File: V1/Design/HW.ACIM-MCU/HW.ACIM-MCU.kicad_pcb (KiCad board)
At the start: 4 copper layers, 39.1 x 39.2 mm, 41 parts, among them J1 HEADER 2x15POS, J2 HEADER 2x15POS, U1 MIPS 32-bit DSC, U2 12MHz (3225), X1 32.768kHz

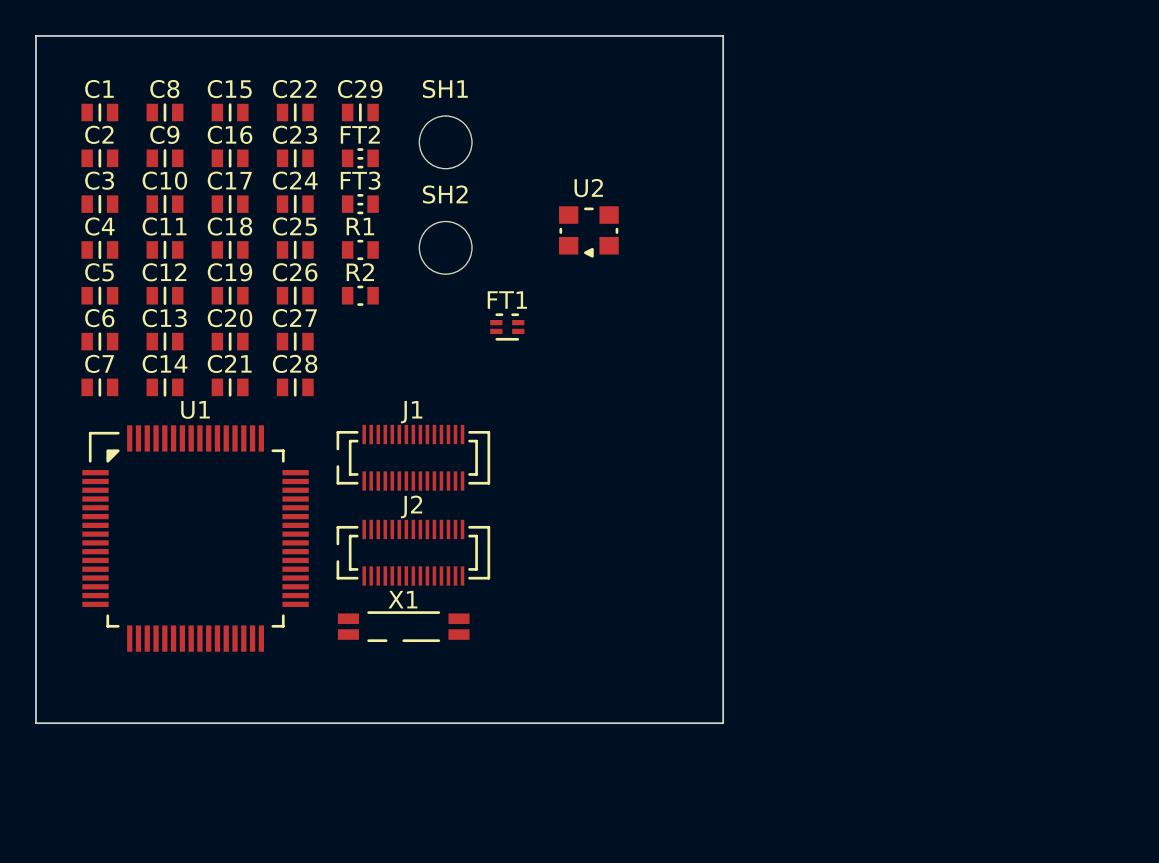
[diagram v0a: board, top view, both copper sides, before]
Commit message: MCU PIM schematic update 3
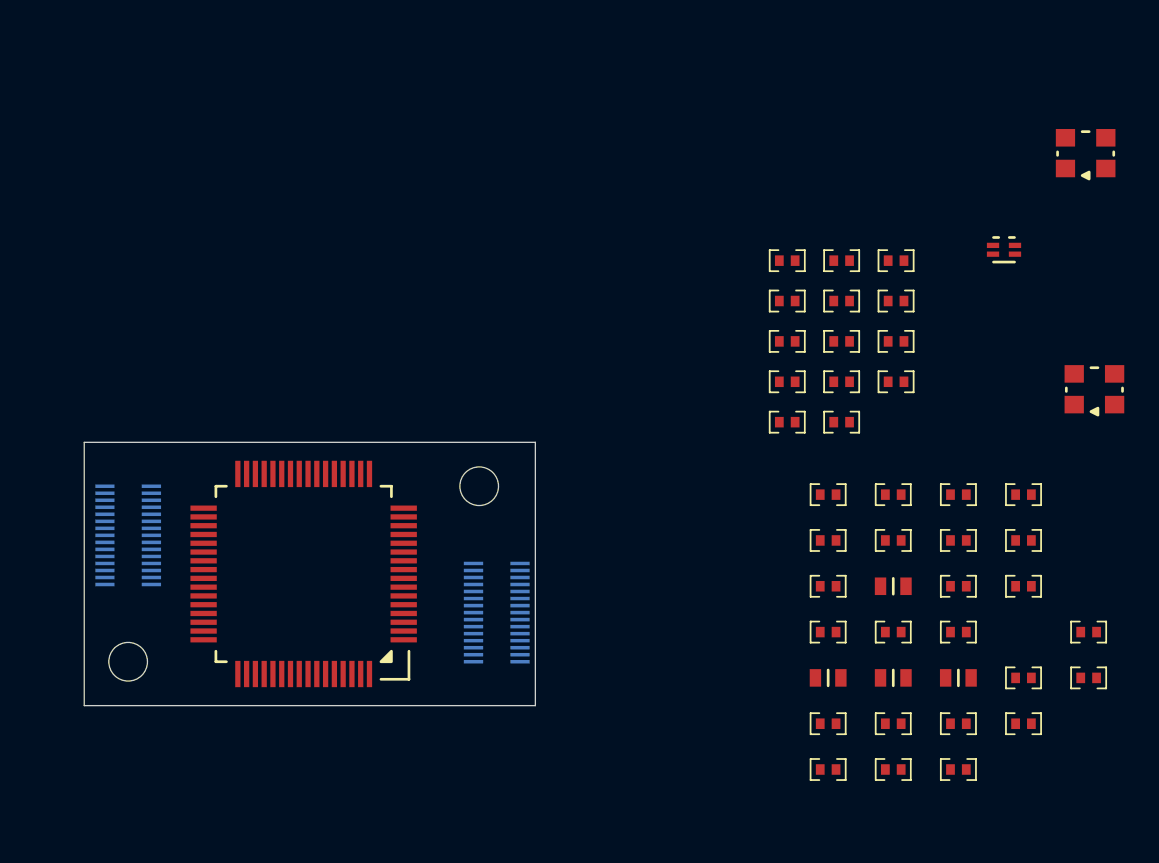
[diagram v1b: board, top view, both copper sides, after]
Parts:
- removed C25: 22pF, SAMPI:CAP0603
- removed C28, C29: 9pF, SAMPI:CAP0603
- removed FT2, FT3: 120R@100MHz, SAMPI:FT0603
- removed X1: 32.768kHz, SAMPI:SMD4-7015
- added R10: 10R, SAMPI:RES0402, F.Cu at (128.0, 90.9)
- added R11: 10R, SAMPI:RES0402, F.Cu at (128.0, 93.2)
- added R12: 10R, SAMPI:RES0402, F.Cu at (128.0, 95.5)
- added R13: 10R, SAMPI:RES0402, F.Cu at (131.1, 86.3)
- added R14: 10R, SAMPI:RES0402, F.Cu at (131.1, 88.6)
- added R15: 10K, SAMPI:RES0402, F.Cu at (131.1, 90.9)
- added R16: 10R, SAMPI:RES0402, F.Cu at (131.1, 93.2)
- added R3: 10R, SAMPI:RES0402, F.Cu at (124.9, 86.3)
- added R4: 10R, SAMPI:RES0402, F.Cu at (124.9, 88.6)
- added R5: 10R, SAMPI:RES0402, F.Cu at (124.9, 90.9)
- added R6: 10R, SAMPI:RES0402, F.Cu at (124.9, 93.2)
- added R7: 10R, SAMPI:RES0402, F.Cu at (124.9, 95.5)
- added R8: 10R, SAMPI:RES0402, F.Cu at (128.0, 86.3)
- added R9: 10R, SAMPI:RES0402, F.Cu at (128.0, 88.6)
- added U3: 32.768kHz, SAMPI:CDFN3225-4LD-PL-1, F.Cu at (142.4, 93.7)
- C1, C11, C13, C14, C15, C17, C18, C2, C20, C21, C22, C23, C24, C26, C27, C3, C4, C6, C7, C8, C9: footprint SAMPI:CAP0603 -> SAMPI:CAP0402
- C12, C5: value 22pF -> 15pF
- C16: value 22pF -> 100nF; footprint SAMPI:CAP0603 -> SAMPI:CAP0402
- J1, J2: moved to B.Cu
- R1: value 0R -> 10K; footprint SAMPI:RES0603 -> SAMPI:RES0402
- R2: value 100K -> 10R; footprint SAMPI:RES0603 -> SAMPI:RES0402
- SH1, SH2: footprint Liem:HOLDER-3MM -> Liem:HOLDER-2.2MM
- U2: value 12MHz (3225) -> 24MHz
- moved C10 46.9 mm to (130.9, 104.9)
- moved C11 46.9 mm to (130.9, 107.5)
- moved C8 46.9 mm to (130.9, 99.6)
- moved C9 46.9 mm to (130.9, 102.2)
- moved R1 46.9 mm to (142.1, 107.5)
- moved C1 46.9 mm to (127.2, 99.6)
- moved C12 46.9 mm to (130.9, 110.1)
- moved C13 46.9 mm to (130.9, 112.7)
- moved C14 46.9 mm to (130.9, 115.3)
- moved C15 46.9 mm to (134.6, 99.6)
- moved C16 46.9 mm to (134.6, 102.2)
- moved C17 46.9 mm to (134.6, 104.9)
- moved C18 46.9 mm to (134.6, 107.5)
- moved C2 46.9 mm to (127.2, 102.2)
- moved C22 46.9 mm to (138.3, 99.6)
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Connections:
- C1 pad 2: /VREF_SENSE -> /VAC_DIV
- C10 pad 1: GND -> AGND
- C10 pad 2: Net-(U1-AVDD) -> AVDD
- C11 pad 2: VDD -> +3V3
- C12 pad 2: Net-(U1-AVDD) -> /RTC_CLK
- C13 pad 2: VDD -> +3V3
- C15 pad 2: /MC_IPM_TEMP -> /MC_IW
- C16 pad 2: VREF -> +3V3
- C17 pad 2: /MC_IU_SENSE -> /MC_IV
- C18 pad 2: /MC_VDC_SENSE -> /MC_VV_DIV
- C19 pad 2: VDD -> +3V3
- C2 pad 2: /PFC_IA_SENSE -> /PFC_IB
- C20 pad 2: /MC_IV_SENSE -> /MC_IU
- C21 pad 2: /MC_VU_SENSE -> /MC_VU_DIV
- C22 pad 1: GND -> AGND
- C22 pad 2: VDD -> /MC_VR_DIV
- C23 pad 2: /MC_IW_SENSE -> /MC_TEMP
- C24 pad 2: /MC_VV_SENSE -> /MC_VDC_DIV
- C26 pad 2: /MC_IDC_SENSE -> /MC_VW_DIV
- C27 pad 2: /MC_VW_SENSE -> /MC_IDC_DIV
- C3 pad 2: /PFC_IB_SENSE -> /PFC_IA
- C4 pad 2: /VAC_SENSE -> /VREF_DIV
- C7 pad 2: VDD -> +3V3
- C8 pad 2: VDD -> +3V3
- C9 pad 2: Net-(U1-AVDD) -> AVDD
- J1 pad 1: unconnected-(J1-Pad1) -> GND
- J1 pad 10: unconnected-(J1-Pad10) -> /TXD1
- J1 pad 11: unconnected-(J1-Pad11) -> /RXD2
- J1 pad 12: unconnected-(J1-Pad12) -> /TXD2
- J1 pad 13: unconnected-(J1-Pad13) -> /IND_ERR
- J1 pad 14: unconnected-(J1-Pad14) -> /IND_RUN
- J1 pad 15: unconnected-(J1-Pad15) -> /MC_PWM_WL
- J1 pad 16: unconnected-(J1-Pad16) -> /MC_PWM_WH
- J1 pad 17: unconnected-(J1-Pad17) -> /MC_PWM_VL
- J1 pad 18: unconnected-(J1-Pad18) -> /MC_PWM_VH
- J1 pad 19: unconnected-(J1-Pad19) -> /MC_PWM_UL
- J1 pad 2: unconnected-(J1-Pad2) -> /PGD
- J1 pad 20: unconnected-(J1-Pad20) -> /MC_PWM_UH
- J1 pad 21: unconnected-(J1-Pad21) -> /~{INV_FLT}
- J1 pad 22: unconnected-(J1-Pad22) -> /MC_VR_SENSE
- J1 pad 23: unconnected-(J1-Pad23) -> /VREF_SENSE
- J1 pad 24: unconnected-(J1-Pad24) -> /MC_TEMP_SENSE
- J1 pad 25: unconnected-(J1-Pad25) -> /MC_IU_SENSE
- J1 pad 26: unconnected-(J1-Pad26) -> /MC_VW_SENSE
- J1 pad 27: unconnected-(J1-Pad27) -> /MC_IV_SENSE
- J1 pad 28: unconnected-(J1-Pad28) -> /MC_VV_SENSE
- J1 pad 29: unconnected-(J1-Pad29) -> /MC_IW_SENSE
- J1 pad 3: unconnected-(J1-Pad3) -> /USB_P
- J1 pad 30: unconnected-(J1-Pad30) -> /MC_VU_SENSE
- J1 pad 4: unconnected-(J1-Pad4) -> /PGC
- J1 pad 5: unconnected-(J1-Pad5) -> /USB_N
- J1 pad 6: unconnected-(J1-Pad6) -> /~{MCLR}
- J1 pad 7: unconnected-(J1-Pad7) -> /VBUS
- J1 pad 8: unconnected-(J1-Pad8) -> /~{BT_UBT}
- J1 pad 9: unconnected-(J1-Pad9) -> /RXD1
- J2 pad 1: unconnected-(J2-Pad1) -> GND
- J2 pad 11: unconnected-(J2-Pad11) -> /SDO
- J2 pad 12: unconnected-(J2-Pad12) -> /SDI
- J2 pad 13: unconnected-(J2-Pad13) -> /~{MEM_CFG}
- J2 pad 14: unconnected-(J2-Pad14) -> /SCK
- J2 pad 15: unconnected-(J2-Pad15) -> /GPIO2
- J2 pad 16: unconnected-(J2-Pad16) -> /GPIO1
- J2 pad 17: unconnected-(J2-Pad17) -> /PFC_PWM_ENB
- J2 pad 18: unconnected-(J2-Pad18) -> /PFC_PWM_B
- J2 pad 19: unconnected-(J2-Pad19) -> /PFC_PWM_ENA
- J2 pad 2: unconnected-(J2-Pad2) -> GND
- J2 pad 20: unconnected-(J2-Pad20) -> /PFC_PWM_A
- J2 pad 21: unconnected-(J2-Pad21) -> /PFC_IA_SENSE
- J2 pad 22: unconnected-(J2-Pad22) -> /~{PFC_FLT}
- J2 pad 23: unconnected-(J2-Pad23) -> /VAC_SENSE
- J2 pad 24: unconnected-(J2-Pad24) -> /PFC_IB_SENSE
- J2 pad 25: unconnected-(J2-Pad25) -> /MC_VDC_SENSE
- J2 pad 26: unconnected-(J2-Pad26) -> /MC_IDC_SENSE
- J2 pad 27: unconnected-(J2-Pad27) -> /ENC_HOME
- J2 pad 28: unconnected-(J2-Pad28) -> /ENC_A
- J2 pad 29: unconnected-(J2-Pad29) -> /ENC_INDEX
- J2 pad 3: unconnected-(J2-Pad3) -> +3V3
- J2 pad 30: unconnected-(J2-Pad30) -> /ENC_B
- J2 pad 4: unconnected-(J2-Pad4) -> +3V3
- J2 pad 5: unconnected-(J2-Pad5) -> AGND
- J2 pad 6: unconnected-(J2-Pad6) -> AGND
- J2 pad 7: unconnected-(J2-Pad7) -> VREF
- J2 pad 8: unconnected-(J2-Pad8) -> VREF
- R1 pad 1: /SYS_CLK -> Net-(U2-EN)
- R1 pad 2: Net-(U2-CLKO) -> +3V3
- R2 pad 1: /VBUS -> /MC_TEMP_SENSE
- R2 pad 2: GND -> /MC_TEMP
- U1 pad 1: /IND_RUN -> unconnected-(U1-TCK/RPA7/PWM10H/PWM4L/PMD5/RA7-Pad1)
- U1 pad 10: VDD -> +3V3
- U1 pad 11: /MC_VDC_SENSE -> /MC_TEMP
- U1 pad 12: /MC_IDC_SENSE -> /PFC_IA
- U1 pad 13: /MC_IU_SENSE -> /PFC_IB
- U1 pad 14: /MC_IV_SENSE -> /MC_IU
- U1 pad 15: /MC_IW_SENSE -> /MC_IV
- U1 pad 16: /MC_VU_SENSE -> /MC_IW
- U1 pad 19: Net-(U1-AVDD) -> AVDD
- U1 pad 21: /MC_VW_SENSE -> /MC_VV_DIV
- U1 pad 22: /MC_VV_SENSE -> /MC_VU_DIV
- U1 pad 23: /MC_IPM_TEMP -> /MC_VW_DIV
- U1 pad 24: /VREF_SENSE -> /VREF_DIV
- U1 pad 26: VDD -> +3V3
- U1 pad 27: /PFC_IA_SENSE -> unconnected-(U1-AN12/CVD12/C2IN2-/C5IN2-/SDA4/FLT5/PMA11/RE12-Pad27)
- U1 pad 28: /PFC_IB_SENSE -> unconnected-(U1-AN13/CVD13/C3IN2-/FLT6/SCL4/PMA10/RE13-Pad28)
- U1 pad 32: /~{MEM_TMP} -> unconnected-(U1-FLT15/RPB4/SCL2/PMA8/RB4-Pad32)
- U1 pad 33: /~{MEM_CFG} -> /MC_VR_DIV
- U1 pad 35: VDD -> +3V3
- U1 pad 38: VDD -> +3V3
- U1 pad 40: /SYS_CLK_EN -> unconnected-(U1-OSCO/CLKO/RPC15/RC15-Pad40)
- U1 pad 42: /~{BT_UBT} -> unconnected-(U1-RD8-Pad42)
- U1 pad 45: /TXD2 -> /MC_VDC_DIV
- U1 pad 46: /TXD1 -> /VAC_DIV
- U1 pad 47: /SOSCI -> /RTC_CLK
- U1 pad 48: /SOSCO -> unconnected-(U1-SOSCO/T1CK/RPB8/RB8-Pad48)
- U1 pad 49: /VAC_SENSE -> /MC_IDC
- U1 pad 57: VDD -> +3V3
- U1 pad 64: /IND_ERR -> unconnected-(U1-TDO/PWM4H/PMD4/RA10-Pad64)
- U2 pad 1: /SYS_CLK_EN -> Net-(U2-EN)
- U2 pad 3: Net-(U2-CLKO) -> /SYS_CLK
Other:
- board size 39.1 x 39.2 mm -> 25.7 x 15 mm

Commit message: MCU PIM schematic update 4
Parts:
- removed FT1: 2x 120R@100MHz, SAMPI:IND1210_4P
- removed R15: 10K, SAMPI:RES0402
- removed R16: 10R, SAMPI:RES0402
- removed U3: 32.768kHz, SAMPI:CDFN3225-4LD-PL-1
- added C25: 100nF, SAMPI:CAP0402, F.Cu at (121.9, 99.4)
- added C28: 10uF, SAMPI:CAP0402, F.Cu at (120.7, 102.1)
- C10: value 10uF -> 100nF; footprint SAMPI:CAP0603 -> SAMPI:CAP0402
- C11, C16, C6, C7, C8, C9: value 100nF -> 22pF
- C12: value 15pF -> 100nF; footprint SAMPI:CAP0603 -> SAMPI:CAP0402
- C13: value 100nF -> 10uF
- C19: value 10uF -> 22pF; footprint SAMPI:CAP0603 -> SAMPI:CAP0402
- C21, C23, C27: value 22pF -> 100nF
- C22, C24, C26: value 22pF -> 10uF
- C5: value 15pF -> 22pF; footprint SAMPI:CAP0603 -> SAMPI:CAP0402
- R1: value 10K -> 10R
- U2: value 24MHz -> 12MHz; footprint SAMPI:CDFN3225-4LD-PL-1 -> SAMPI:SMD4-2520
- moved U2 37.6 mm to (111.6, 102.5), turned to 180 degrees
- moved J2 26.9 mm to (113.6, 107.6)
- moved J1 23.6 mm to (86.6, 97.3)
- moved SH2 8.18 mm to (114.2, 94.8)
- moved U1 3.35 mm to (100.3, 102.7), turned to 0 degrees
- moved SH1 1.66 mm to (86.4, 110.6)
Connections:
- C1 pad 2: /VAC_DIV -> /MC_IW
- C10 pad 1: AGND -> GND
- C10 pad 2: AVDD -> +3V3
- C11 pad 2: +3V3 -> /VBUS
- C12 pad 1: GND -> AGND
- C12 pad 2: /RTC_CLK -> AVDD
- C13 pad 1: GND -> AGND
- C13 pad 2: +3V3 -> AVDD
- C14 pad 1: GND -> AGND
- C14 pad 2: /VBUS -> /VAC_DIV
- C15 pad 2: /MC_IW -> /PFC_IB
- C16 pad 1: GND -> AGND
- C16 pad 2: +3V3 -> /PFC_IA
- C17 pad 2: /MC_IV -> /VREF_DIV
- C18 pad 2: /MC_VV_DIV -> /MC_VW_DIV
- C19 pad 2: +3V3 -> Net-(U1-OSCI/CLKI/AN49/CVD49/RPC12/RC12)
- C2 pad 2: /PFC_IB -> /MC_IV
- C20 pad 1: AGND -> GND
- C20 pad 2: /MC_IU -> Net-(U1-OSCO/CLKO/RPC15/RC15)
- C21 pad 1: AGND -> GND
- C21 pad 2: /MC_VU_DIV -> +3V3
- C22 pad 1: AGND -> GND
- C22 pad 2: /MC_VR_DIV -> +3V3
- C23 pad 1: AGND -> GND
- C23 pad 2: /MC_TEMP -> +3V3
- C24 pad 1: AGND -> GND
- C24 pad 2: /MC_VDC_DIV -> +3V3
- C26 pad 1: AGND -> GND
- C26 pad 2: /MC_VW_DIV -> +3V3
- C27 pad 1: AGND -> GND
- C27 pad 2: /MC_IDC_DIV -> +3V3
- C3 pad 2: /PFC_IA -> /MC_IU
- C4 pad 2: /VREF_DIV -> /MC_TEMP
- C5 pad 1: GND -> AGND
- C5 pad 2: /SYS_CLK -> /MC_VV_DIV
- C6 pad 1: GND -> AGND
- C6 pad 2: +3V3 -> /MC_VU_DIV
- C7 pad 1: GND -> AGND
- C7 pad 2: +3V3 -> /MC_VDC_DIV
- C8 pad 1: GND -> AGND
- C8 pad 2: +3V3 -> /MC_IDC_DIV
- C9 pad 2: AVDD -> /MC_VR_DIV
- J1 pad 10: /TXD1 -> unconnected-(J1-Pad10)
- J1 pad 11: /RXD2 -> /SDO
- J1 pad 12: /TXD2 -> /SDI
- J1 pad 13: /IND_ERR -> /~{MEM_CFG}
- J1 pad 14: /IND_RUN -> /SCK
- J1 pad 15: /MC_PWM_WL -> /GPIO2
- J1 pad 16: /MC_PWM_WH -> /GPIO1
- J1 pad 17: /MC_PWM_VL -> /PFC_PWM_ENB
- J1 pad 18: /MC_PWM_VH -> /PFC_PWM_B
- J1 pad 19: /MC_PWM_UL -> /PFC_PWM_ENA
- J1 pad 2: /PGD -> GND
- J1 pad 20: /MC_PWM_UH -> /PFC_PWM_A
- J1 pad 21: /~{INV_FLT} -> /PFC_IA_SENSE
- J1 pad 22: /MC_VR_SENSE -> /~{PFC_FLT}
- J1 pad 23: /VREF_SENSE -> /VAC_SENSE
- J1 pad 24: /MC_TEMP_SENSE -> /PFC_IB_SENSE
- J1 pad 25: /MC_IU_SENSE -> /MC_VDC_SENSE
- J1 pad 26: /MC_VW_SENSE -> /MC_IDC_SENSE
- J1 pad 27: /MC_IV_SENSE -> /ENC_HOME
- J1 pad 28: /MC_VV_SENSE -> /ENC_A
- J1 pad 29: /MC_IW_SENSE -> /ENC_INDEX
- J1 pad 3: /USB_P -> +3V3
- J1 pad 30: /MC_VU_SENSE -> /ENC_B
- J1 pad 4: /PGC -> +3V3
- J1 pad 5: /USB_N -> AGND
- J1 pad 6: /~{MCLR} -> AGND
- J1 pad 7: /VBUS -> VREF
- J1 pad 8: /~{BT_UBT} -> VREF
- J1 pad 9: /RXD1 -> unconnected-(J1-Pad9)
- J2 pad 10: unconnected-(J2-Pad10) -> /TXD1
- J2 pad 11: /SDO -> /RXD2
- J2 pad 12: /SDI -> /TXD2
- J2 pad 13: /~{MEM_CFG} -> /IND_ERR
- J2 pad 14: /SCK -> /IND_RUN
- J2 pad 15: /GPIO2 -> /MC_PWM_WL
- J2 pad 16: /GPIO1 -> /MC_PWM_WH
- J2 pad 17: /PFC_PWM_ENB -> /MC_PWM_VL
- J2 pad 18: /PFC_PWM_B -> /MC_PWM_VH
- J2 pad 19: /PFC_PWM_ENA -> /MC_PWM_UL
- J2 pad 2: GND -> /PGD
- J2 pad 20: /PFC_PWM_A -> /MC_PWM_UH
- J2 pad 21: /PFC_IA_SENSE -> /~{INV_FLT}
- J2 pad 22: /~{PFC_FLT} -> /MC_VR_SENSE
- J2 pad 23: /VAC_SENSE -> /VREF_SENSE
- J2 pad 24: /PFC_IB_SENSE -> /MC_TEMP_SENSE
- J2 pad 25: /MC_VDC_SENSE -> /MC_IU_SENSE
- J2 pad 26: /MC_IDC_SENSE -> /MC_VW_SENSE
- J2 pad 27: /ENC_HOME -> /MC_IV_SENSE
- J2 pad 28: /ENC_A -> /MC_VV_SENSE
- J2 pad 29: /ENC_INDEX -> /MC_IW_SENSE
- J2 pad 3: +3V3 -> /USB_P
- J2 pad 30: /ENC_B -> /MC_VU_SENSE
- J2 pad 4: +3V3 -> /PGC
- J2 pad 5: AGND -> /USB_N
- J2 pad 6: AGND -> /~{MCLR}
- J2 pad 7: VREF -> /VBUS
- J2 pad 8: VREF -> /~{BT_UBT}
- J2 pad 9: unconnected-(J2-Pad9) -> /RXD1
- R1 pad 1: Net-(U2-EN) -> /MC_TEMP_SENSE
- R1 pad 2: +3V3 -> /MC_TEMP
- R2 pad 1: /MC_TEMP_SENSE -> /MC_IU_SENSE
- R2 pad 2: /MC_TEMP -> /MC_IU
- R3 pad 1: /MC_IU_SENSE -> /MC_IV_SENSE
- R3 pad 2: /MC_IU -> /MC_IV
- R4 pad 1: /MC_IV_SENSE -> /MC_IW_SENSE
- R4 pad 2: /MC_IV -> /MC_IW
- R5 pad 1: /MC_IW_SENSE -> /MC_VR_SENSE
- R5 pad 2: /MC_IW -> /MC_VR_DIV
- U1 pad 36: /USB1_N -> /USB_N
- U1 pad 37: /USB1_P -> /USB_P
- U1 pad 39: /SYS_CLK -> Net-(U1-OSCI/CLKI/AN49/CVD49/RPC12/RC12)
- U1 pad 40: unconnected-(U1-OSCO/CLKO/RPC15/RC15-Pad40) -> Net-(U1-OSCO/CLKO/RPC15/RC15)
- U1 pad 47: /RTC_CLK -> unconnected-(U1-SOSCI/RPC13/RC13-Pad47)
- U2 pad 1: Net-(U2-EN) -> Net-(U1-OSCI/CLKI/AN49/CVD49/RPC12/RC12)
- U2 pad 3: /SYS_CLK -> Net-(U1-OSCO/CLKO/RPC15/RC15)
- U2 pad 4: +3V3 -> GND
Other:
- board size 25.7 x 15 mm -> 32 x 20 mm

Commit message: MCU PIM schematic update 5
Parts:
- removed C1, C11, C14, C15, C16, C17, C18, C2, C3, C4, C5, C6, C7, C8, C9: 22pF, SAMPI:CAP0402
- removed R1, R10, R11, R12, R13, R14, R2, R3, R4, R5, R6, R7, R8, R9: 10R, SAMPI:RES0402
- removed SH1, SH2: SCREW HOLDER, Liem:HOLDER-2.2MM
- C10, C12, C13, C19, C20, C21, C22, C23, C24, C25, C26, C27, C28, U1, U2: moved to B.Cu
- J1, J2: footprint SAMPI:HD-2x15x0.4-SMD -> SAMPI:HD-2x15x1.27-TH
- moved U2 13.6 mm to (125.2, 101.3), turned to 0 degrees
- moved C25 11.6 mm to (132.8, 95.2), turned to 180 degrees
- moved C28 11.6 mm to (131.5, 98.0), turned to 180 degrees
- moved J1 5.35 mm to (86.4, 102.7)
- moved J2 4.95 mm to (114.3, 102.7)
- turned C10 to 180 degrees
- turned C12 to 180 degrees
- turned C13 to 180 degrees
- turned C19 to 180 degrees
- turned C20 to 180 degrees
- turned C21 to 180 degrees
- turned C22 to 180 degrees
- turned C23 to 180 degrees
- turned C24 to 180 degrees
- turned C26 to 180 degrees
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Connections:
- net /~{MEM_CFG} renamed /~{CS}
- J1 pad 10: unconnected-(J1-Pad10) -> /IO3
- J1 pad 11: /SDO -> /IO0
- J1 pad 12: /SDI -> /IO1
- J1 pad 14: /SCK -> /SDI
- J1 pad 15: /GPIO2 -> /SDO
- J1 pad 16: /GPIO1 -> /SCK
- J1 pad 21: /PFC_IA_SENSE -> /PFC_IA_SEN
- J1 pad 23: /VAC_SENSE -> /VAC_DIV
- J1 pad 24: /PFC_IB_SENSE -> /PFC_IB_SEN
- J1 pad 25: /MC_VDC_SENSE -> /MC_VDC_DIV
- J1 pad 26: /MC_IDC_SENSE -> /MC_IDC_SEN
- J1 pad 9: unconnected-(J1-Pad9) -> /IO2
- J2 pad 22: /MC_VR_SENSE -> /MC_VR_DIV
- J2 pad 23: /VREF_SENSE -> /VREF_DIV
- J2 pad 24: /MC_TEMP_SENSE -> /MC_TEMP_SEN
- J2 pad 25: /MC_IU_SENSE -> /MC_IU_SEN
- J2 pad 26: /MC_VW_SENSE -> /MC_VW_DIV
- J2 pad 27: /MC_IV_SENSE -> /MC_IV_SEN
- J2 pad 28: /MC_VV_SENSE -> /MC_VV_DIV
- J2 pad 29: /MC_IW_SENSE -> /MC_IW_SEN
- J2 pad 30: /MC_VU_SENSE -> /MC_VU_DIV
- U1 pad 11: /MC_TEMP -> /MC_TEMP_SEN
